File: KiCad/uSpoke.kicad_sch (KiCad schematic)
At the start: 71 parts, among them J1 SM12B-SRSS-TB, J12 Amphenol 132289, J2 PLS-1x4, J4 PLS-1x3, Q2 AO3407A, Q3 AO3400, Q5 AO3400, SW1 SW-SPST-2P, SW2 SW-SPST-2P, SW3 SW-SPST-2P, SW4 SW-SPST-2P, U1 SP0503BAHTG, U2 MCP73831T-2ACI/OT, U4 LM3671MF-3.3, U5 74HC4052PW, U6 STM32F103C8T6, X1 8MHz

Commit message: Update PCB
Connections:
- net +BATT: now also U2.3 (VBAT); no longer U2.6 (VBAT)
- net BOOT0: now also SW1.2; no longer SW1.4 (1)
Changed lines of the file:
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@@
 	)
 	(junction
-		(at 232.41 203.2)
+		(at 311.15 96.52)
 		(diameter 0)
 		(color 0 0 0 0)
 	)
 	(junction
-		(at 311.15 96.52)
+		(at 232.41 200.66)
 		(diameter 0)
 		(color 0 0 0 0)
@@
 	(wire
 		(pts
+			(xy 232.41 200.66) (xy 232.41 205.74)
+		)
+		(stroke
+			(width 0)
+			(type default)
+		)
+	)
+	(wire
+		(pts
 			(xy 525.78 228.6) (xy 532.13 228.6)
 		)
@@
 	(wire
 		(pts
-			(xy 232.41 203.2) (xy 232.41 205.74)
-		)
-		(stroke
-			(width 0)
-			(type default)
-		)
-	)
-	(wire
-		(pts
 			(xy 231.14 369.57) (xy 231.14 370.84)
 		)
@@
 	(wire
 		(pts
-			(xy 232.41 198.12) (xy 232.41 203.2)
+			(xy 232.41 198.12) (xy 232.41 200.66)
 		)
 		(stroke
@@
 	(wire
 		(pts
-			(xy 215.9 203.2) (xy 232.41 203.2)
-		)
-		(stroke
-			(width 0)
-			(type default)
-		)
-	)
-	(wire
-		(pts
 			(xy 334.01 71.12) (xy 337.82 71.12)
 		)
@@
 	(wire
 		(pts
+			(xy 215.9 200.66) (xy 232.41 200.66)
+		)
+		(stroke
+			(width 0)
+			(type default)
+		)
+	)
+	(wire
+		(pts
 			(xy 331.47 132.08) (xy 331.47 143.51)
 		)
@@
 		(pin "1"
 		)
-		(pin "6"
+		(pin "3"
 		)
 		(pin "5"

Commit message: Prettify SCH
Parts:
- removed SW3: SW-SPST-2P, uSpoke:TL3330AF260QG, symbol uSpoke:SW-SPST-2P
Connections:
- net BTN_ESC is gone; now on net BOOT0: U6.39 (PB3)
- net BUZZ_N is gone; now on net BUZZER_N: D3.1, D3.2, Q5.3 (D), R29.1
- net VEXT is gone; now on net VBUS: C1.2, R10.2, U2.4 (VDD)
- net +3V3: now also C28.1, C30.1, J1.11, J1.8
- net +BATT: now also J1.1, J1.2
- net CONSOLE_RXD_EXT: now also J2.3, U1.4 (K)
- net CONSOLE_TXD_EXT: now also J2.2, U1.3 (K)
- net GND: now also C28.2, C30.2, J1.3, J1.4, J1.9, J2.4, SW1.3 (1), SW1.4 (1), SW2.3 (1), SW2.4 (1), SW4.3 (1), SW4.4 (1), U1.1 (A)
- net GPS_PPS: now also J1.7
- net GPS_RXD: now also J1.6
- net GPS_TXD: now also J1.5
- net I2C_SCL: now also TP1.1; no longer TP2.1
- net I2C_SDA: now also TP2.1; no longer TP1.1
- net MOVE_SW: now also J1.10
- net BUZZER_N: now reaches J1.12
- net VBUS: now reaches U1.2 (K)
- net VBUS: now also J2.1
- net BUZZER renamed BUZZER_PWM
- no-connect marks 4 -> 11
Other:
- note added: "BAT V+"
- note added: "BAT V-"
- note added: "BUZZER+"
- note added: "BUZZER-"
- note added: "GPS GND"
- note added: "GPS PPS"
- note added: "GPS RX"
- note added: "GPS TX"
- note added: "GPS VCC"
- note added: "MOVE SW"
- note removed: "BAT V+ BAT V+ BAT GND BAT GND GPS TX GPS RX GPS PPS GPS V+ GPS GND BUZZ+ BUZZ- MOVE+"
- note removed: "EVQ-P7A01P"
- note removed: "Single Li-Ion cell DOUBLE CHECK CELL PINOUT BEFORE CONNECT!"
- note removed: "TL3330AF260QG"
- moved on the sheet: A1, A2, C1, C11, C13, C14, C15, C16, C17, C18, C19, C20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

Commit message: Fix ERC
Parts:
- A1: symbol Spoke:E104-BT5005A -> uSpoke:E104-BT5005A
- A2: symbol Spoke:E22-400M22S -> uSpoke:E22-400M22S
- C1, C11, C13, C15, C16, C17, C18, C19, C20, C22, C23, C27, C30, C5, C8: symbol Spoke:C -> uSpoke:C
- C14, C25, C26, C28: symbol Spoke:C-Polar -> uSpoke:C-Polar
- D1, D3: symbol Spoke:BAT54C -> uSpoke:BAT54C
- D2, D4, D5: symbol Spoke:LED -> uSpoke:LED
- J12: symbol Spoke:SMA-Connector -> uSpoke:SMA-Connector
- J4: symbol Spoke:PLS-1x3 -> uSpoke:PLS-1x3
- L1: symbol Spoke:L -> uSpoke:L
- Q2: symbol Spoke:PMOS -> uSpoke:PMOS
- Q3, Q5: symbol Spoke:NMOS -> uSpoke:NMOS
- R1, R10, R11, R12, R13, R15, R17, R23, R26, R27, R28, R29, R3, R32, R33, R34, R4, R5, R6, R7, R8, R9: symbol Spoke:R -> uSpoke:R
- TP1, TP10, TP11, TP2, TP3: symbol Spoke:Pad-Round -> uSpoke:Pad-Round
- U4: symbol Spoke:LM3671MF-3.3 -> uSpoke:LM3671MF-3.3
- U5: symbol Spoke:74HC4052PW -> uSpoke:74HC4052PW
- U6: symbol Spoke:STM32F103C8T6 -> uSpoke:STM32F103C8T6
- X1: symbol Spoke:Xtal-4pin -> uSpoke:Xtal-4pin
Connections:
- net BOOT0 renamed BOOT0/BTN_ESC
- no-connect marks 11 -> 15
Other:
- moved on the sheet: A1, A2, C1, C11, C13, C14, C15, C16, C17, C18, C19, C20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

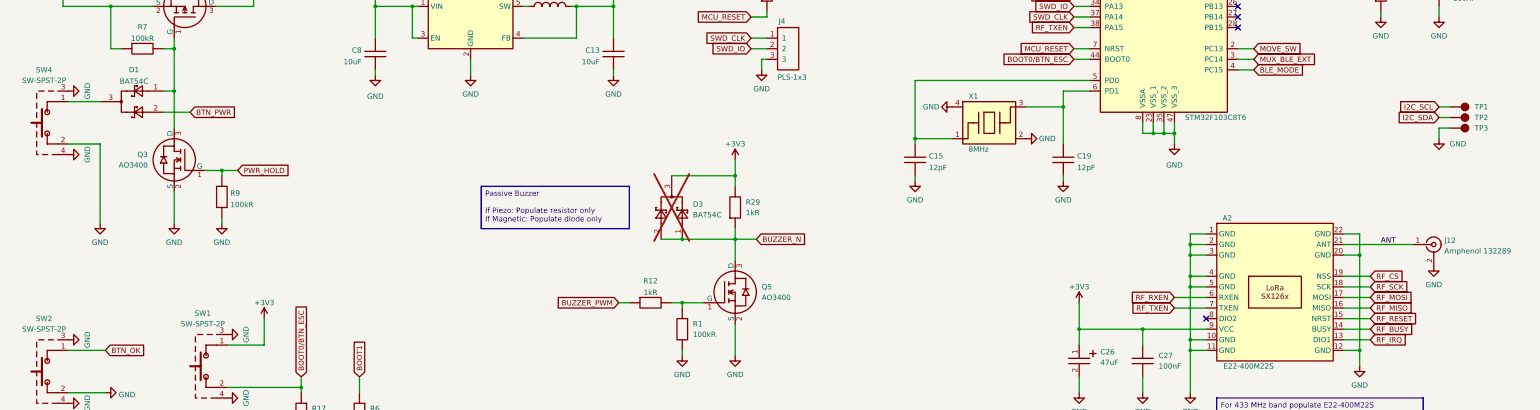
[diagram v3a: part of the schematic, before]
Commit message: Update SCH and lib links
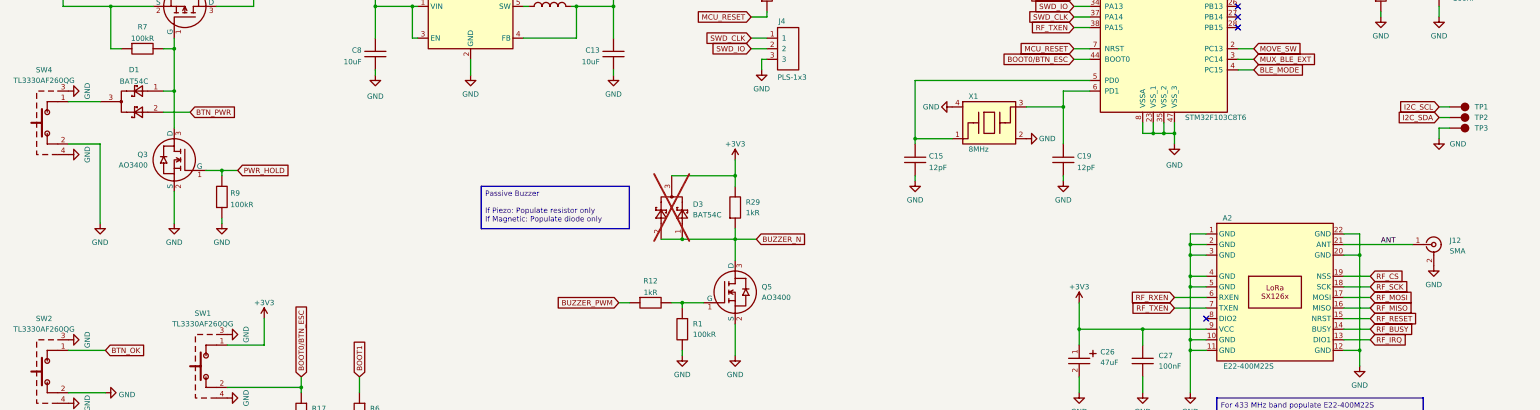
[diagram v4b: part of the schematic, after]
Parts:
- A1: footprint uSpoke:E104-BT5005A -> (none)
- A2: footprint uSpoke:E22 -> (none)
- C1, C13, C5, C8: footprint uSpoke:C0805 -> (none)
- C11, C15, C16, C17, C18, C19, C20, C22, C23, C27, C30: footprint uSpoke:C0603 -> (none)
- C14, C25, C26, C28: footprint uSpoke:C_tantA -> (none)
- D1, D3, Q2, Q3, Q5: footprint uSpoke:SOT-23 -> (none)
- D2, D4, D5: footprint uSpoke:LED0603 -> (none)
- J1: footprint uSpoke:SM12B-SRSS-TB -> (none)
- J12: value Amphenol 132289 -> SMA; footprint uSpoke:SMA -> (none)
- J2: footprint uSpoke:Header_1x4 -> (none)
- J4: footprint uSpoke:Header_1x3 -> (none)
- L1: footprint uSpoke:L1616 -> (none)
- R1, R10, R11, R12, R13, R15, R17, R23, R26, R27, R28, R29, R3, R32, R33, R34, R4, R5, R6, R7, R8, R9: footprint uSpoke:R0603 -> (none)
- SW1, SW2, SW4: value SW-SPST-2P -> TL3330AF260QG; symbol uSpoke:SW-SPST-2P -> uSpoke:TL3330AF260QG
- TP1, TP10, TP11, TP2, TP3: footprint uSpoke:Pad_round -> (none)
- U1: footprint uSpoke:SOT-143 -> (none)
- U2, U4: footprint uSpoke:SOT-23-5 -> (none)
- U5: footprint uSpoke:TSSOP-16 -> (none)
- U6: footprint uSpoke:LQFP-48 -> (none)
- X1: footprint uSpoke:Xtal_3225 -> (none)

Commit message: Clean PCB lib
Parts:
- A1: footprint (none) -> uSpoke:E104-BT5005A
- A2: footprint (none) -> uSpoke:E22
- C1, C13, C5, C8: footprint (none) -> uSpoke:C0805
- C11, C15, C16, C17, C18, C19, C20, C22, C23, C27, C30: footprint (none) -> uSpoke:C0603
- C14, C25, C26, C28: footprint (none) -> uSpoke:C_tantA
- D1, D3, Q2, Q3, Q5: footprint (none) -> uSpoke:SOT-23
- D2, D4, D5: footprint (none) -> uSpoke:LED0603
- J1: footprint (none) -> uSpoke:SM12B-SRSS-TB
- J12: footprint (none) -> uSpoke:SMA
- J2: footprint (none) -> uSpoke:Header_1x4
- J4: footprint (none) -> uSpoke:Header_1x3
- L1: footprint (none) -> uSpoke:L1616
- R1, R10, R11, R12, R13, R15, R17, R23, R26, R27, R28, R29, R3, R32, R33, R34, R4, R5, R6, R7, R8, R9: footprint (none) -> uSpoke:R0603
- TP1, TP10, TP11, TP2, TP3: footprint (none) -> uSpoke:Pad_round
- U1: footprint (none) -> uSpoke:SOT-143
- U2, U4: footprint (none) -> uSpoke:SOT-23-5
- U5: footprint (none) -> uSpoke:TSSOP-16
- U6: footprint (none) -> uSpoke:LQFP-48
- X1: footprint (none) -> uSpoke:Xtal_3225
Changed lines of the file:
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@@
 			)
 		)
-		(property "Footprint" ""
+		(property "Footprint" "uSpoke:R0603"
 			(at 190.5 245.11 0)
 			(effects
@@
 			)
 		)
-		(property "Footprint" ""
+		(property "Footprint" "uSpoke:R0603"
 			(at 54.61 91.44 0)
 			(effects
@@
 			)
 		)
-		(property "Footprint" ""
+		(property "Footprint" "uSpoke:LED0603"
 			(at 379.73 40.64 0)
 			(effects
@@
 			)
 		)
-		(property "Footprint" ""
+		(property "Footprint" "uSpoke:Pad_round"
 			(at 370.84 120.65 0)
 			(effects
@@
 			)
 		)
-		(property "Footprint" ""
+		(property "Footprint" "uSpoke:SOT-23"
 			(at 186.69 149.86 0)
 			(effects
@@
 			)
 		)
-		(property "Footprint" ""
+		(property "Footprint" "uSpoke:Header_1x3"
 			(at 207.01 101.6 0)
 			(effects
@@
 			)
 		)
-		(property "Footprint" ""
+		(property "Footprint" "uSpoke:C0603"
 			(at 355.6 86.36 0)
 			(effects
@@
 			)
 		)
-		(property "Footprint" ""
+		(property "Footprint" "uSpoke:C0603"
 			(at 264.16 35.56 0)
 			(effects
@@
 			)
 		)
-		(property "Footprint" ""
+		(property "Footprint" "uSpoke:SOT-23"
 			(at 80.01 104.14 0)
 			(effects
@@
 			)
 		)
-		(property "Footprint" ""
+		(property "Footprint" "uSpoke:R0603"
 			(at 257.81 208.28 0)
 			(effects
@@
 			)
 		)
-		(property "Footprint" ""
+		(property "Footprint" "uSpoke:C0603"
 			(at 289.56 35.56 0)
 			(effects
@@
 			)
 		)
-		(property "Footprint" ""
+		(property "Footprint" "uSpoke:TSSOP-16"
 			(at 160.02 218.44 0)
 			(effects
@@
 			)
 		)
-		(property "Footprint" ""
+		(property "Footprint" "uSpoke:C0603"
 			(at 265.43 127 0)
 			(effects
@@
 			)
 		)
-		(property "Footprint" ""
+		(property "Footprint" "uSpoke:R0603"
 			(at 245.11 77.47 0)
 			(effects
@@
 			)
 		)
-		(property "Footprint" ""
+		(property "Footprint" "uSpoke:R0603"
 			(at 190.5 254 0)
 			(effects
@@
 			)
 		)
-		(property "Footprint" ""
+		(property "Footprint" "uSpoke:R0603"
 			(at 360.68 27.94 0)
 			(effects
@@
 			)
 		)
-		(property "Footprint" ""
+		(property "Footprint" "uSpoke:C0805"
 			(at 90.17 53.34 0)
 			(effects
@@
 			)
 		)
-		(property "Footprint" ""
+		(property "Footprint" "uSpoke:R0603"
 			(at 341.63 92.71 0)
 			(effects
@@
 			)
 		)
-		(property "Footprint" ""
+		(property "Footprint" "uSpoke:R0603"
 			(at 341.63 80.01 0)
 			(effects
@@
 			)
 		)
-		(property "Footprint" ""
+		(property "Footprint" "uSpoke:SOT-23-5"
 			(at 123.19 93.98 0)
 			(effects
@@
 			)
 		)
-		(property "Footprint" ""
+		(property "Footprint" "uSpoke:Pad_round"
 			(at 370.84 118.11 0)
 			(effects
@@
 			)
 		)
-		(property "Footprint" ""
+		(property "Footprint" "uSpoke:Xtal_3225"
 			(at 251.46 125.73 0)
 			(effects
@@
 			)
 		)
-		(property "Footprint" ""
+		(property "Footprint" "uSpoke:C_tantA"
 			(at 102.87 226.06 0)
 			(effects
@@
 			)
 		)
-		(property "Footprint" ""
+		(property "Footprint" "uSpoke:C0603"
 			(at 284.48 175.26 0)
 			(effects
@@
 			)
 		)
-		(property "Footprint" ""
+		(property "Footprint" "uSpoke:LED0603"
 			(at 128.27 49.53 0)
 			(effects
@@
 			)
 		)
-		(property "Footprint" ""
+		(property "Footprint" "uSpoke:R0603"
 			(at 176.53 152.4 0)
 			(effects
@@
 			)
 		)
-		(property "Footprint" ""
+		(property "Footprint" "uSpoke:C0805"
 			(at 100.33 109.22 0)
 			(effects
@@
 			)
 		)
-		(property "Footprint" ""
+		(property "Footprint" "uSpoke:R0603"
 			(at 186.69 144.78 0)
 			(effects
@@
 			)
 		)
-		(property "Footprint" ""
+		(property "Footprint" "uSpoke:R0603"
 			(at 171.45 48.26 0)
 			(effects
@@
 			)
 		)
-		(property "Footprint" ""
+		(property "Footprint" "uSpoke:C0603"
 			(at 302.26 35.56 0)
 			(effects
@@
 			)
 		)
-		(property "Footprint" ""
+		(property "Footprint" "uSpoke:R0603"
 			(at 107.95 189.23 0)
 			(effects
@@
 			)
 		)
-		(property "Footprint" ""
+		(property "Footprint" "uSpoke:C0603"
 			(at 293.37 220.98 0)
 			(effects
@@
 			)
 		)
-		(property "Footprint" ""
+		(property "Footprint" "uSpoke:SM12B-SRSS-TB"
 			(at 54.61 233.68 0)
 			(effects
@@
 			)
 		)
-		(property "Footprint" ""
+		(property "Footprint" "uSpoke:Pad_round"
 			(at 370.84 123.19 0)
 			(effects
@@
 			)
 		)
-		(property "Footprint" ""
+		(property "Footprint" "uSpoke:SOT-143"
 			(at 49.53 44.45 0)
 			(effects
@@
 			)
 		)
-		(property "Footprint" ""
+		(property "Footprint" "uSpoke:C0603"
 			(at 176.53 200.66 0)
 			(effects
@@
 			)
 		)
-		(property "Footprint" ""
+		(property "Footprint" "uSpoke:C_tantA"
 			(at 332.74 220.98 0)
 			(effects
@@
 			)
 		)
-		(property "Footprint" ""
+		(property "Footprint" "uSpoke:C0603"
 			(at 229.87 127 0)
 			(effects
@@
 			)
 		)
-		(property "Footprint" ""
+		(property "Footprint" "uSpoke:Pad_round"
 			(at 290.83 231.14 0)
 			(effects
@@
 			)
 		)
-		(property "Footprint" ""
+		(property "Footprint" "uSpoke:E22"
 			(at 312.42 148.59 0)
 			(effects
@@
 			)
 		)
-		(property "Footprint" ""
+		(property "Footprint" "uSpoke:C0805"
 			(at 157.48 109.22 0)
 			(effects
@@
 			)
 		)
-		(property "Footprint" ""
+		(property "Footprint" "uSpoke:SOT-23"
 			(at 74.93 118.11 0)
 			(effects
@@
 			)
 		)
-		(property "Footprint" ""
+		(property "Footprint" "uSpoke:R0603"
 			(at 63.5 142.24 0)
 			(effects
@@
 			)
 		)
-		(property "Footprint" ""
+		(property "Footprint" "uSpoke:L1616"
 			(at 149.86 93.98 0)
 			(effects
@@
 			)
 		)
-		(property "Footprint" ""
+		(property "Footprint" "uSpoke:C0603"
 			(at 276.86 35.56 0)
 			(effects
@@
 			)
 		)
-		(property "Footprint" ""
+		(property "Footprint" "uSpoke:R0603"
 			(at 121.92 189.23 0)
 			(effects
@@
 			)
 		)
-		(property "Footprint" ""
+		(property "Footprint" "uSpoke:SOT-23-5"
 			(at 129.54 39.37 0)
 			(effects
@@
 			)
 		)
-		(property "Footprint" ""
+		(property "Footprint" "uSpoke:R0603"
 			(at 157.48 209.55 0)
 			(effects
@@
 			)
 		)
-		(property "Footprint" ""
+		(property "Footprint" "uSpoke:R0603"
 			(at 137.16 254 0)
 			(effects
@@
 			)
 		)
-		(property "Footprint" ""
+		(property "Footprint" "uSpoke:R0603"
 			(at 199.39 168.91 0)
 			(effects
@@
 			)
 		)
-		(property "Footprint" ""
+		(property "Footprint" "uSpoke:SOT-23"
 			(at 189.23 149.86 0)
 			(effects
@@
 			)
 		)
-		(property "Footprint" ""
+		(property "Footprint" "uSpoke:C_tantA"
 			(at 294.64 175.26 0)
 			(effects
@@
 			)
 		)
-		(property "Footprint" ""
+		(property "Footprint" "uSpoke:SMA"
 			(at 361.95 151.13 0)
 			(effects
@@
 			)
 		)
-		(property "Footprint" ""
+		(property "Footprint" "uSpoke:R0603"
 			(at 360.68 40.64 0)
 			(effects
@@
 			)
 		)
-		(property "Footprint" ""
+		(property "Footprint" "uSpoke:LED0603"
 			(at 379.73 53.34 0)
 			(effects
@@
 			)
 		)
-		(property "Footprint" ""
+		(property "Footprint" "uSpoke:E104-BT5005A"
 			(at 255.27 215.9 0)
 			(effects
@@
 			)
 		)
-		(property "Footprint" ""
+		(property "Footprint" "uSpoke:C_tantA"
 			(at 243.84 36.83 0)
 			(effects
@@
 			)
 		)
-		(property "Footprint" ""
+		(property "Footprint" "uSpoke:C0603"
 			(at 62.23 226.06 0)
 			(effects
@@
 			)
 		)
-		(property "Footprint" ""
+		(property "Footprint" "uSpoke:SOT-23"
 			(at 62.23 114.3 0)
 			(effects
@@
 			)
 		)
-		(property "Footprint" ""
+		(property "Footprint" "uSpoke:LQFP-48"
 			(at 284.48 63.5 0)
 			(effects
@@
 			)
 		)
-		(property "Footprint" ""
+		(property "Footprint" "uSpoke:Pad_round"
 			(at 290.83 233.68 0)
 			(effects
@@
 			)
 		)
-		(property "Footprint" ""
+		(property "Footprint" "uSpoke:R0603"
 			(at 137.16 245.11 0)
 			(effects
@@
 			)
 		)
-		(property "Footprint" ""
+		(property "Footprint" "uSpoke:R0603"
 			(at 99.06 46.99 0)
 			(effects
@@
 			)
 		)
-		(property "Footprint" ""
+		(property "Footprint" "uSpoke:Header_1x4"
 			(at 39.37 36.83 0)
 			(effects
@@
 			)
 		)
-		(property "Footprint" ""
+		(property "Footprint" "uSpoke:R0603"
 			(at 245.11 208.28 0)
 			(effects
@@
 			)
 		)
-		(property "Footprint" ""
+		(property "Footprint" "uSpoke:R0603"
 			(at 194.31 92.71 0)
 			(effects
@@
 			)
 		)
-		(property "Footprint" ""
+		(property "Footprint" "uSpoke:C0805"
 			(at 165.1 53.34 0)
 			(effects

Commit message: SCH to PCB sync
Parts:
- removed J1: SM12B-SRSS-TB, uSpoke:SM12B-SRSS-TB, symbol uSpoke:SM12B-SRSS-TB
- added J2: SM12B-SRSS-TB, uSpoke:SM12B-SRSS-TB, symbol uSpoke:SM12B-SRSS-TB
- renumbered C30 to C1, C16 to C10, C17 to C11, C18 to C12, C19 to C13, C26 to C14, C20 to C15, C27 to C16, C23 to C17, C25 to C18, C22 to C19, C28 to C2, C1 to C3, C8 to C4, C11 to C5, C13 to C6, C5 to C7, C14 to C8, C15 to C9, J2 to J1, J4 to J3, J12 to J4, Q2 to Q1, Q3 to Q2, Q5 to Q3, R7 to R1, R12 to R10, R1 to R11, R8 to R12, R11 to R13, R29 to R14, R28 to R16, R32 to R17, R23 to R18, R33 to R19, R9 to R2, R34 to R20, R26 to R21, R27 to R22, R17 to R3, R6 to R4, R10 to R5, R3 to R6, R5 to R7, R13 to R8, R4 to R9, SW4 to SW1, SW1 to SW3, TP10 to TP1, TP11 to TP2, TP1 to TP3, TP2 to TP4, TP3 to TP5, U4 to U2, U2 to U3, U5 to U4, U6 to U5
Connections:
- net +3V3: now also J2.2, J2.5
- net +BATT: now also J2.11, J2.12
- net BUZZER_N: now also J2.1
- net GND: now also J2.10, J2.4, J2.9, J2.MP
- net GPS_PPS: now also J2.6
- net GPS_RXD: now also J2.7
- net GPS_TXD: now also J2.8
- net MOVE_SW: now also J2.3
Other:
- moved on the sheet: C1, C2
